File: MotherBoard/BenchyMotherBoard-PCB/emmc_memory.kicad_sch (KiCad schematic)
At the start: 23 parts, among them J16 Micro_SD_Card_Det1, J4 Micro_SD_Card_Det1, U11 IS21ES08GA-JCLI, U4 AM6254ATCGGAALW

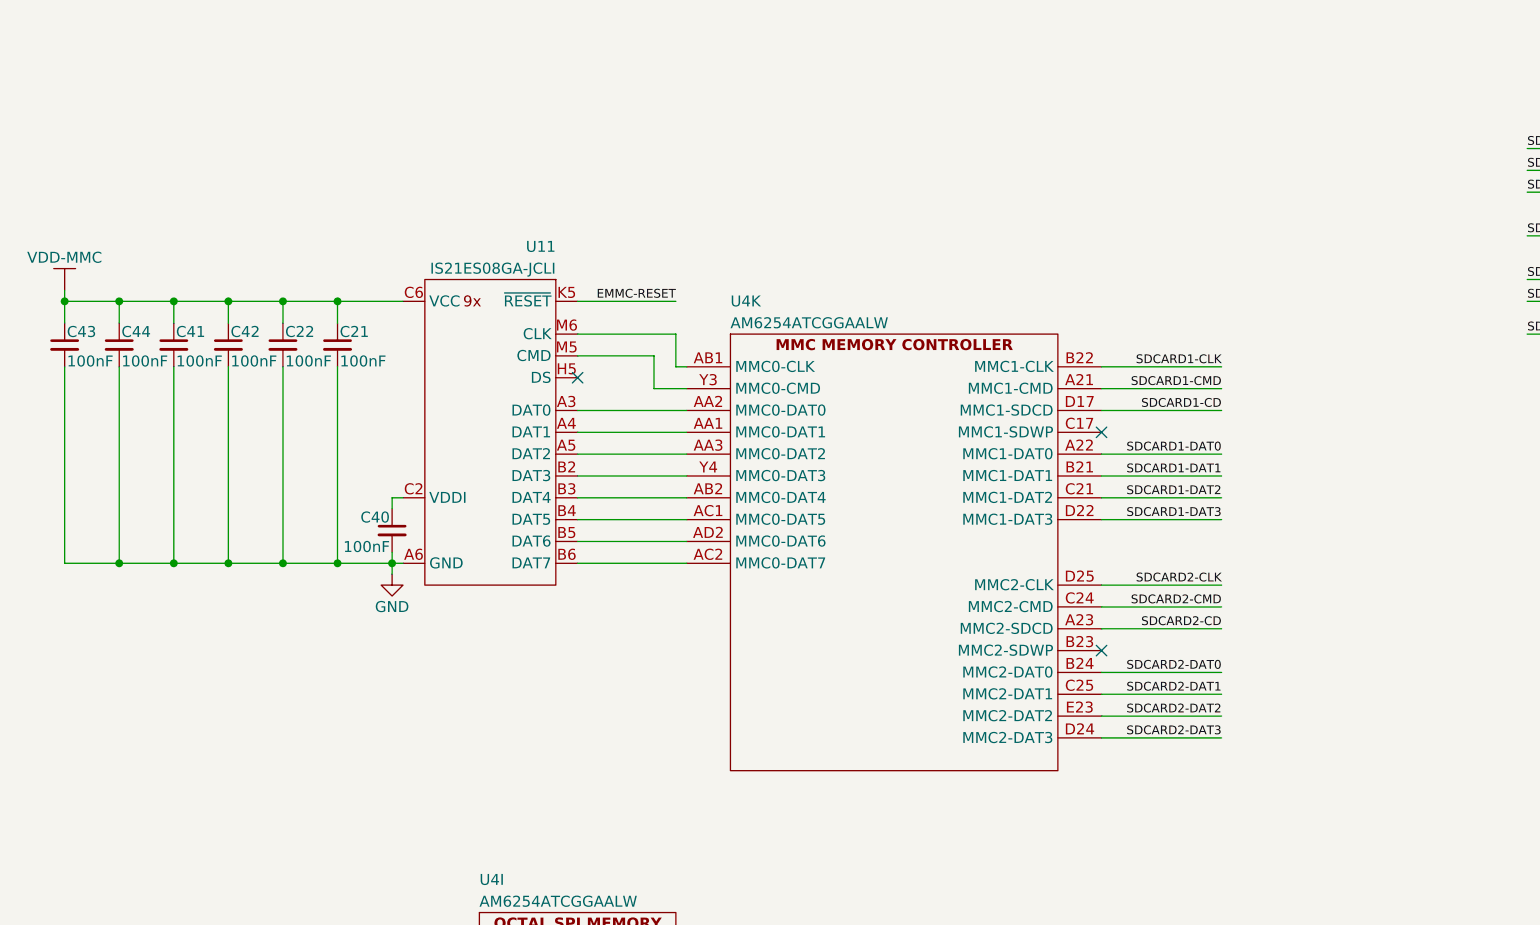
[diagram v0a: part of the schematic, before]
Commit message: (WIP) More work on power supply sequencing
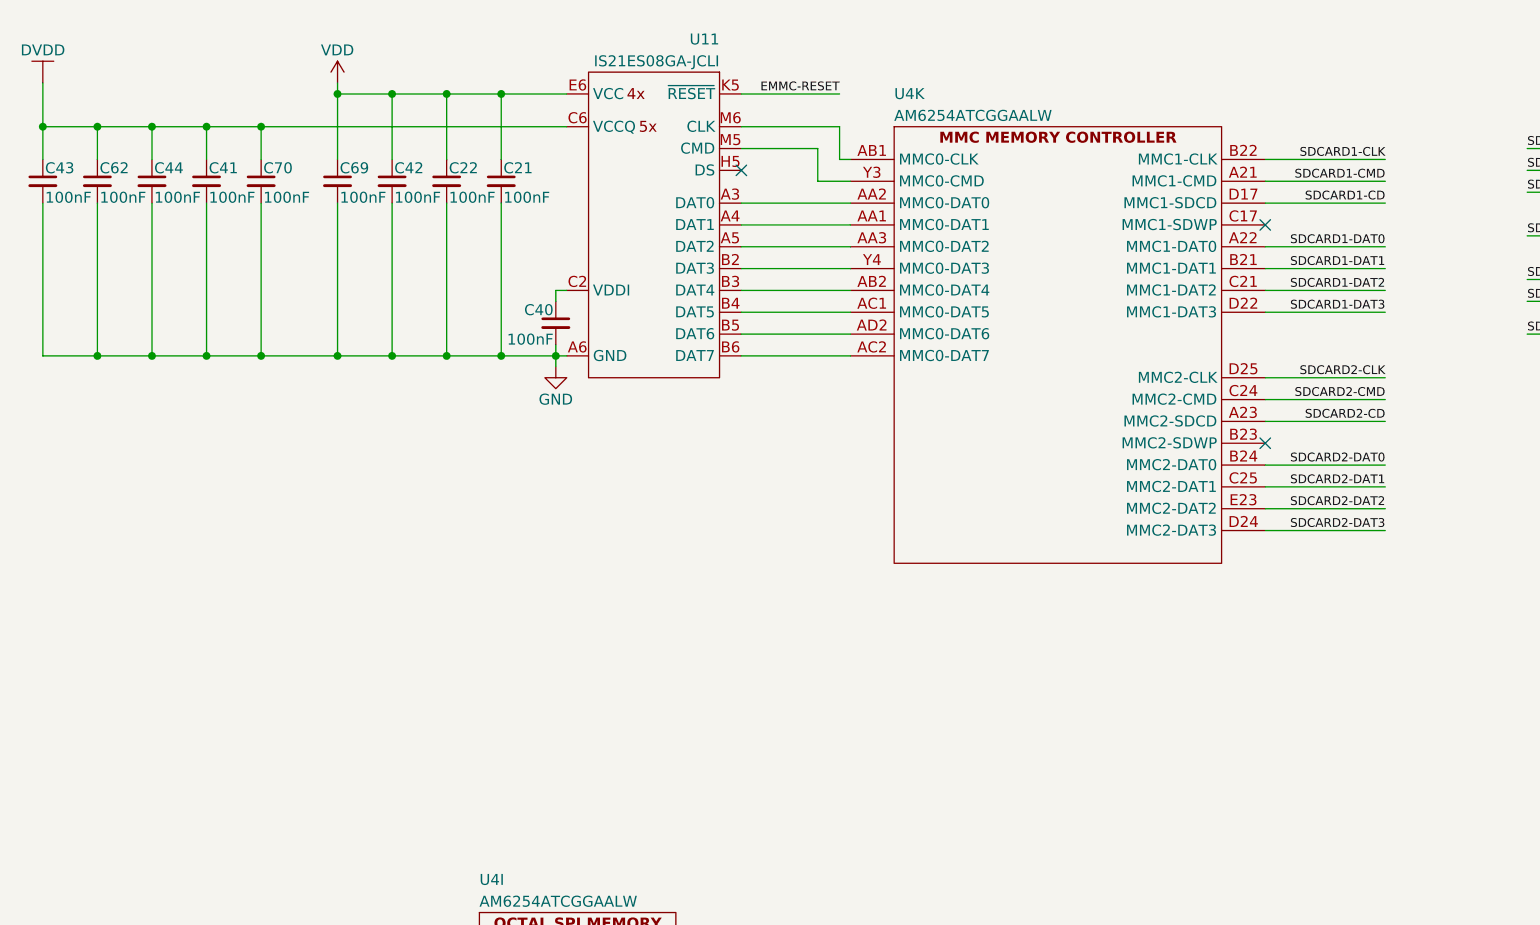
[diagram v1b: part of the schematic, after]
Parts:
- added C62, C69, C70: 100nF, Capacitor_SMD:C_0402_1005Metric, symbol Daxxn_Device:C
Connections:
- net GND: now also C62.2, C69.2, C70.2
- net VDD-MMC: no longer C21.1, C22.1, C41.1, C42.1, C43.1, C44.1, U11.C6 (VCC), U11.E6 (VCC), U11.F5 (VCC), U11.J10 (VCC), U11.K9 (VCC), U11.M4 (VCC), U11.N4 (VCC), U11.P3 (VCC), U11.P5 (VCC)
- new net DVDD: C41.1, C43.1, C44.1, C62.1, C70.1, U11.C6 (VCCQ), U11.M4 (VCCQ), U11.N4 (VCCQ), U11.P3 (VCCQ), U11.P5 (VCCQ)
- new net VDD: C21.1, C22.1, C42.1, C69.1, U11.E6 (VCC), U11.F5 (VCC), U11.J10 (VCC), U11.K9 (VCC)
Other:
- moved on the sheet: C21, C22, C40, C41, C42, C43, C44, U4K

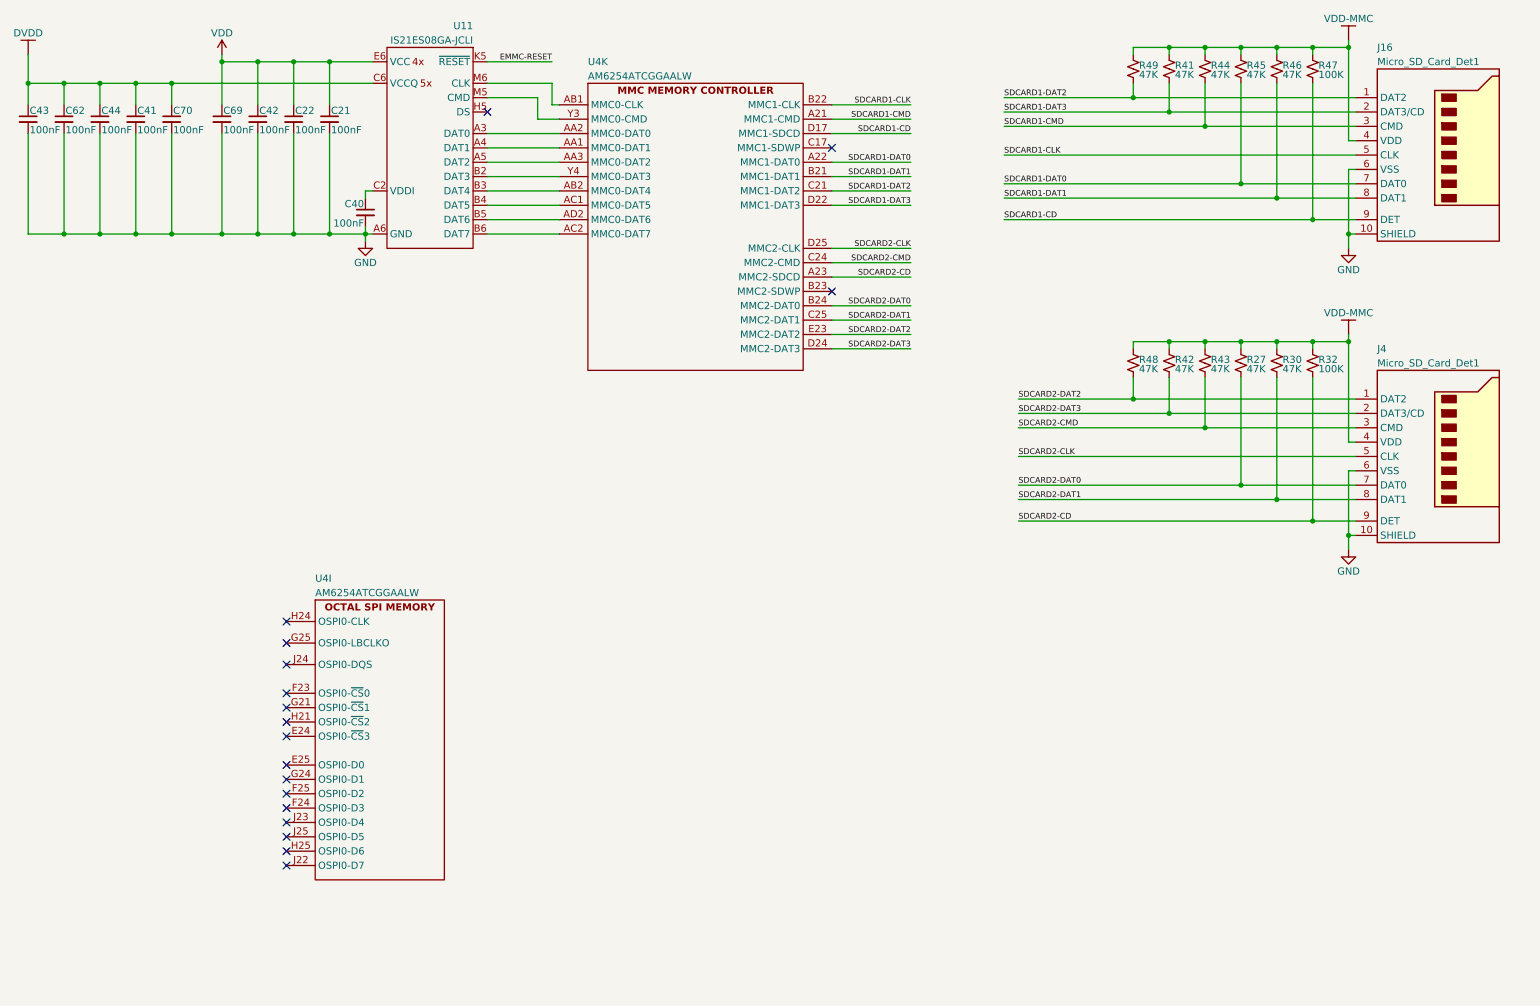
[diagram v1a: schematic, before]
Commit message: (WIP) Complete most of the PS and boot schematics
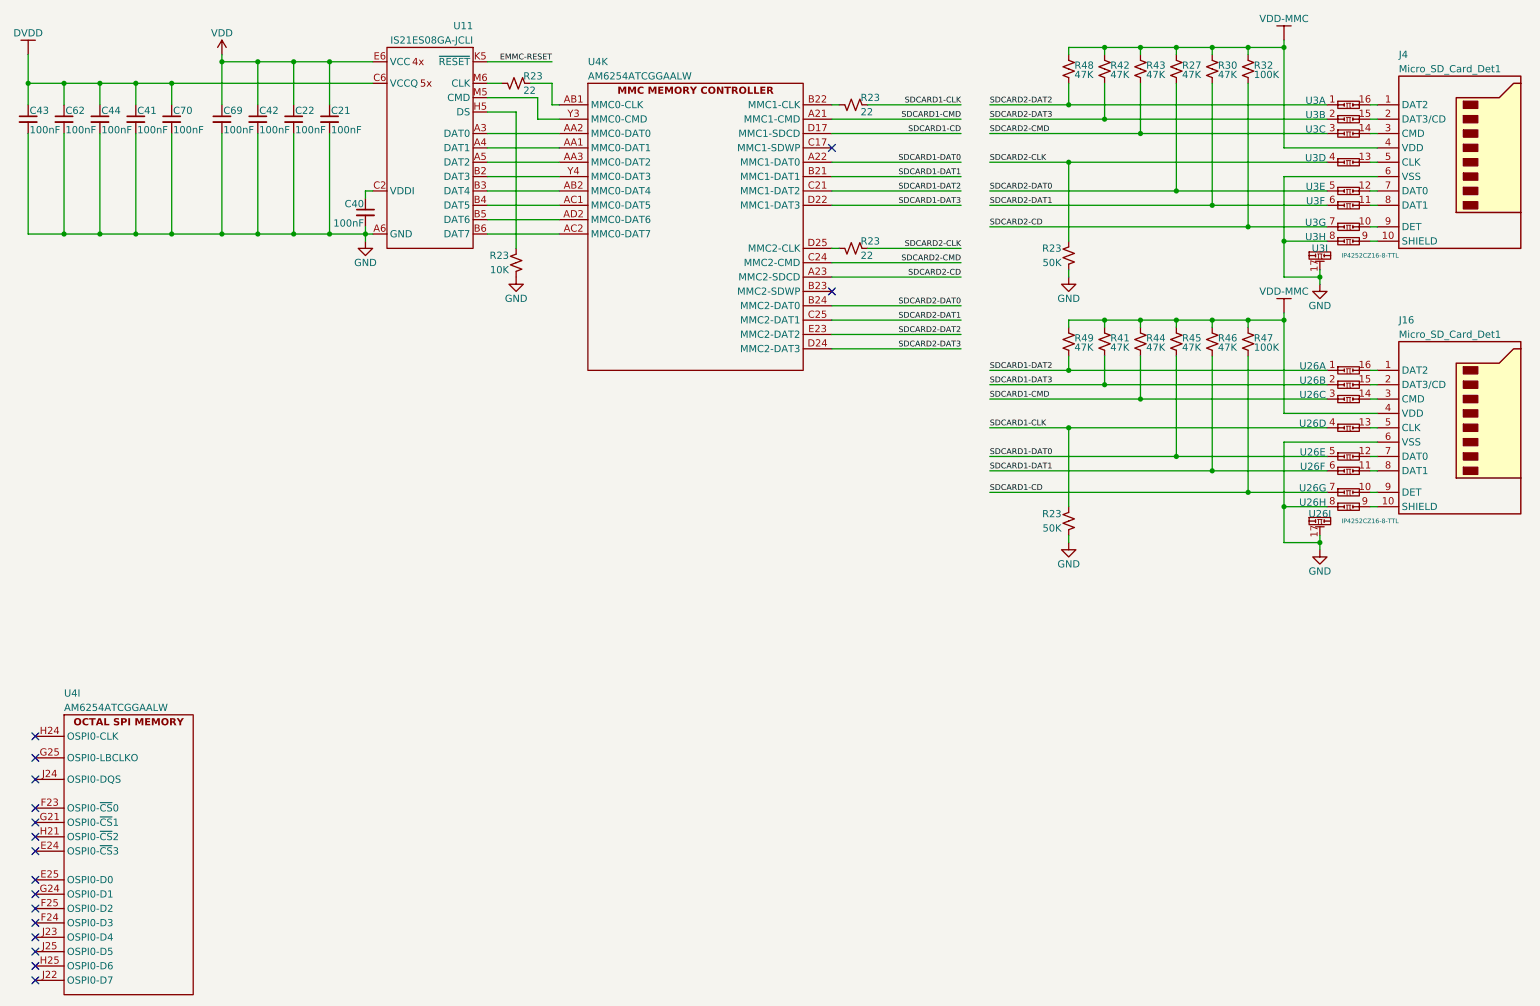
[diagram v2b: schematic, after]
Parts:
- added R23 (x3): 22, Resistor_SMD:R_0201_0603Metric, symbol Daxxn_Device:R
- added R23 (x2): 50K, Resistor_SMD:R_0201_0603Metric, symbol Daxxn_Device:R
- added R23: 10K, Resistor_SMD:R_0201_0603Metric, symbol Daxxn_Device:R
- added U26, U3: IP4252CZ16-8-TTL, Daxxn_Packages:QFN16_SOT1168-1_NEX-M, symbol Daxxn_Protection:IP4252CZ16-8-TTL
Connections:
- net GND: now also R23.2, R23.2, R23.2, U26.17 (GND), U26.8 (8A), U3.17 (GND), U3.8 (8A); no longer J16.10 (SHIELD), J4.10 (SHIELD)
- net SDCARD1-CD: now also U26.7 (7A); no longer J16.9 (DET)
- net SDCARD1-CLK: now also R23.1, R23.1, U26.4 (4A); no longer J16.5 (CLK), U4.B22 (MMC1-CLK)
- net SDCARD1-CMD: now also U26.3 (3A); no longer J16.3 (CMD)
- net SDCARD1-DAT0: now also U26.5 (5A); no longer J16.7 (DAT0)
- net SDCARD1-DAT1: now also U26.6 (6A); no longer J16.8 (DAT1)
- net SDCARD1-DAT2: now also U26.1 (1A); no longer J16.1 (DAT2)
- net SDCARD1-DAT3: now also U26.2 (2A); no longer J16.2 (DAT3/CD)
- net SDCARD2-CD: now also U3.7 (7A); no longer J4.9 (DET)
- net SDCARD2-CLK: now also R23.1, R23.1, U3.4 (4A); no longer J4.5 (CLK), U4.D25 (MMC2-CLK)
- net SDCARD2-CMD: now also U3.3 (3A); no longer J4.3 (CMD)
- net SDCARD2-DAT0: now also U3.5 (5A); no longer J4.7 (DAT0)
- net SDCARD2-DAT1: now also U3.6 (6A); no longer J4.8 (DAT1)
- net SDCARD2-DAT2: now also U3.1 (1A); no longer J4.1 (DAT2)
- net SDCARD2-DAT3: now also U3.2 (2A); no longer J4.2 (DAT3/CD)
- net at U4.AB1 (MMC0-CLK): now also R23.1; no longer U11.M6 (CLK)
- net at U11.H5 (DS): now also R23.1
- new net: R23.2, U11.M6 (CLK)
- new net: J16.9 (DET), U26.10 (7B)
- new net: J4.1 (DAT2), U3.16 (1B)
- new net: J4.10 (SHIELD), U3.9 (8B)
- new net: J4.2 (DAT3/CD), U3.15 (2B)
- new net: J4.3 (CMD), U3.14 (3B)
- new net: J4.5 (CLK), U3.13 (4B)
- new net: J4.7 (DAT0), U3.12 (5B)
- new net: J4.8 (DAT1), U3.11 (6B)
- new net: J4.9 (DET), U3.10 (7B)
- new net: J16.5 (CLK), U26.13 (4B)
- new net: J16.1 (DAT2), U26.16 (1B)
- new net: J16.10 (SHIELD), U26.9 (8B)
- new net: J16.2 (DAT3/CD), U26.15 (2B)
- new net: J16.3 (CMD), U26.14 (3B)
- new net: J16.7 (DAT0), U26.12 (5B)
- new net: J16.8 (DAT1), U26.11 (6B)
- new net: R23.2, U4.B22 (MMC1-CLK)
- new net: R23.2, U4.D25 (MMC2-CLK)
- no-connect marks 18 -> 17
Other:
- moved on the sheet: J16, J4, R27, R30, R32, R41, R42, R43, R44, R45, R46, R47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

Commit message: Add new ethernet chip - KSZ9031
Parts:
- added C158 (x2), C291, C292, C293: 100nF, Capacitor_SMD:C_0402_1005Metric, symbol Daxxn_Device:C
- added C158 (x2), C290: 1uF, Capacitor_SMD:C_0603_1608Metric, symbol Daxxn_Device:C
- added C158 (x2): 4.7uF, Capacitor_SMD:C_0805_2012Metric, symbol Daxxn_Device:C
- added C158 (x3): 100nF, Capacitor_SMD:C_0201_0603Metric, symbol Daxxn_Device:C
- added R102 (x4): 50K, Resistor_SMD:R_0402_1005Metric, symbol Daxxn_Device:R
- added R102 (x6): 10K, Resistor_SMD:R_0402_1005Metric, symbol Daxxn_Device:R
- added R102 (x2): 1K, Resistor_SMD:R_0201_0603Metric, symbol Daxxn_Device:R
- added R102 (x2): 10K, Resistor_SMD:R_0201_0603Metric, symbol Daxxn_Device:R
- added R102 (x5): 22, Resistor_SMD:R_0201_0603Metric, symbol Daxxn_Device:R
- added R102: 100K, Resistor_SMD:R_0201_0603Metric, symbol Daxxn_Device:R
- added U34 (x2): 74HCT2G08, Daxxn_Packages:SOT-353_SC-70-5, symbol Daxxn_Logic:74LVC1G08GW
- added U36: 74HCT2G08, Daxxn_Packages:WSON-6_1.5x1.5mm_P0.5mm, symbol Daxxn_Logic:SN74LVC1G11DRYR
- added U37, U38: SIP32510DT-T1-GE3, Daxxn_Packages:TSOT-23-6, symbol Daxxn_IC:SIP32510DT-T1-GE3
- added U39: S28HS512TGABHI010, Daxxn_Packages:BGA-24_5x5_6.0x8.0mm, symbol Daxxn_Memory:S28HS512TGABHI010
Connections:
- net DVDD: now also C158.1, C158.1, C290.1, C291.1, C292.1, C293.1, R102.2, R102.2, R102.2, R102.2, R102.2, R102.2, R102.2, R102.2, U34.5 (VCC), U34.5 (VCC), U39.B4 (VCC), U39.D1 (VCCQ), U39.E4 (VCCQ)
- net GND: now also C158.2, C158.2, C158.2, C158.2, C158.2, C158.2, C158.2, C158.2, C158.2, C290.2, C291.2, C292.2, C293.2, R102.1, R102.1, R102.1, R102.1, U34.3 (GND), U34.3 (GND), U36.2 (GND), U37.4 (GND), U38.4 (GND), U39.B3 (GND), U39.C1 (GND), U39.E5 (GND)
- net VDD: now also C158.1, R102.2, R102.2, R102.2, U36.5 (VCC)
- net at R23.1, U4.AB1 (MMC0-CLK): now also R102.2
- net at U11.A3 (DAT0), U4.AA2 (MMC0-DAT0): now also R102.1
- net at U11.M5 (CMD), U4.Y3 (MMC0-CMD): now also R102.1
- net OSPI-DQ0: now reaches U4.E25 (OSPI0-D0)
- net OSPI-DQ0: now also U39.D3 (DQ0)
- net OSPI-~{CS}: now reaches U4.F23 (OSPI0-~{CS}0)
- net OSPI-~{CS}: now also R102.1, U39.C2 (~{CS})
- net OSPI-DQ3: now reaches U4.F24 (OSPI0-D3)
- net OSPI-DQ3: now also U39.D4 (DQ3)
- net OSPI-DQ2: now reaches U4.F25 (OSPI0-D2)
- net OSPI-DQ2: now also U39.C4 (DQ2)
- net ~{OSPI-RESET}: now reaches U4.G21 (OSPI0-~{CS}1)
- net ~{OSPI-RESET}: now also R102.1, U34.2 (A)
- net OSPI-DQ1: now reaches U4.G24 (OSPI0-D1)
- net OSPI-DQ1: now also U39.D2 (DQ1)
- net at U4.G25 (OSPI0-LBCLKO): now also R102.1
- net ~{OSPI-INT}: now reaches U4.H21 (OSPI0-~{CS}2)
- net ~{OSPI-INT}: now also R102.1, R102.2
- net OSPI-CLK: now reaches U4.H24 (OSPI0-CLK)
- net OSPI-DQ6: now reaches U4.H25 (OSPI0-D6)
- net OSPI-DQ6: now also U39.E2 (DQ6)
- net OSPI-DQ7: now reaches U4.J22 (OSPI0-D7)
- net OSPI-DQ7: now also U39.E1 (DQ7)
- net OSPI-DQ4: now reaches U4.J23 (OSPI0-D4)
- net OSPI-DQ4: now also U39.D5 (DQ4)
- net OSPI-DQS: now reaches U4.J24 (OSPI0-DQS)
- net OSPI-DQS: now also R102.2, R102.2
- net OSPI-DQ5: now reaches U4.J25 (OSPI0-D5)
- net OSPI-DQ5: now also U39.E3 (DQ5)
- net EMMC-RESET renamed ~{RESET-EMMC}
- net ~{RESET-EMMC}: now also R102.1, U34.4 (Y)
- net VDD-MMC renamed SDCARD1-PWR
- net SDCARD1-PWR: now also C158.1, U37.1 (OUT), U37.2 (OUT); no longer J16.4 (VDD), R41.1, R44.1, R45.1, R46.1, R47.1, R49.1
- new net: R102.1, U39.A5 (~{INT})
- new net: U39.A2 (DNU), U39.A3 (DNU), U39.B1 (DNU), U39.B5 (DNU), U39.C5 (DNU)
- new net: R102.1, R102.2, U39.B2 (CK)
- new net IN: C158.1, C158.1, C158.1, C158.1, U37.5 (IN), U37.6 (IN), U38.5 (IN), U38.6 (IN)
- new net OSPI-CK: R102.2
- new net OSPI-DS: R102.1, R102.1, R102.2, U39.C3 (DS)
- new net OSPI-LBCLK: R102.1, R102.2
- new net SDCARD2-PWR: C158.1, J16.4 (VDD), R41.1, R44.1, R45.1, R46.1, R47.1, R49.1, U38.1 (OUT), U38.2 (OUT)
- new net ~{EMMC-RESET}: R102.1, R102.2, U34.1 (B)
- new net ~{POR-OUT}: U36.3 (B)
- new net ~{RESET-OSPI}: R102.1, U34.4 (Y), U39.A4 (~{RESET})
- new net ~{RESET-SDCARD1}: R102.1, U36.4 (Y), U37.3 (EN), U38.3 (EN)
- new net ~{RESET-STATUS}: U34.1 (B), U34.2 (A), U36.1 (A)
- new net ~{SDCARD1-EN}: R102.1, U36.6 (C)
- no-connect marks 17 -> 3
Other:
- moved on the sheet: C21, C22, C40, C41, C42, C43, C44, C62, C69, C70, J16, J4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

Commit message: (WIP) Almost done with schematic
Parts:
- added C158: 100nF, Capacitor_SMD:C_0201_0603Metric, symbol Daxxn_Device:C
- added C158 (x2): 100nF, Capacitor_SMD:C_0402_1005Metric, symbol Daxxn_Device:C
- added C389, C390, C391: 2.2uF, Capacitor_SMD:C_0805_2012Metric, symbol Daxxn_Device:C
- added R102 (x2): 10K, Resistor_SMD:R_0402_1005Metric, symbol Daxxn_Device:R
- added U30: 74HCT2G08, Daxxn_Packages:WSON-6_1.5x1.5mm_P0.5mm, symbol Daxxn_Logic:SN74LVC1G11DRYR
- R102, R23: value 50K -> 49.9K
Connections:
- net DVDD: now also C389.1, C391.1
- net GND: now also C158.2, C158.2, C158.2, C389.2, C390.2, C391.2, U30.2 (GND)
- net SDCARD1-PWR: now also C158.1
- net SDCARD2-PWR: now also C158.1
- net VDD: now also C158.1, C390.1, R102.2, R102.2, U30.5 (VCC)
- net ~{EMMC-RESET}: now also R102.1, U11.K5 (~{RESET}), U34.4 (Y); no longer R102.1, R102.2, U34.1 (B)
- net ~{OSPI-RESET}: now also R102.1, U34.4 (Y); no longer R102.1, U34.2 (A)
- net ~{POR-OUT}: now also U30.3 (B)
- net ~{RESET-EMMC}: now also R102.1, R102.2, U34.1 (B); no longer R102.1, U11.K5 (~{RESET}), U34.4 (Y)
- net ~{RESET-OSPI}: now also R102.1, U34.2 (A); no longer R102.1, U34.4 (Y)
- net ~{RESET-SDCARD1}: no longer U38.3 (EN)
- net ~{RESET-STATUS}: now also U30.1 (A)
- new net ~{RESET-SDCARD2}: R102.1, U30.4 (Y), U38.3 (EN)
- new net ~{SDCARD2-EN}: R102.1, U30.6 (C)
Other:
- moved on the sheet: C158, C21, C22, C40, C41, C42, C43, C44, C62, C69, C70, R102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

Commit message: Start PCB layout
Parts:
- renumbered C389 to C430, C43 to C431, C62 to C432, C44 to C433, C41 to C434, C70 to C435, C390 to C436, C69 to C437, C42 to C438, C22 to C439, C21 to C440, C391 to C441, C290 to C442, C291 to C443, C292 to C444, C293 to C445, C40 to C446, J4 to J24, J16 to J25, R48 to R298, R42 to R299, R43 to R300, R27 to R301, R30 to R302, R32 to R303, R49 to R304, R41 to R305, R44 to R306, R45 to R307, R46 to R308, R47 to R309, U11 to U52, U39 to U53, U37 to U54, U38 to U55, U3 to U56, U26 to U57, U36 to U59, U30 to U60
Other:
- moved on the sheet: C158, R102, U34, U59, U60
